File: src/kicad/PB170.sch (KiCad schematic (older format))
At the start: 51 parts, among them J2 USB_B_Micro, Q1 BC817, Q2 BC817, Q3 BC817, Q4 BC817, SW1 SW_MEC_5E, U1 74HC08, U20 74LS73, U21 74LS73

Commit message: Partially fixed footprint library and reassigning references
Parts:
- C1: footprint Capacitors_SMD:C_0805 -> Capacitor_SMD:C_0805_2012Metric
- C2: footprint Capacitors_SMD:C_1206 -> Capacitor_SMD:C_1206_3216Metric
- C3: footprint Capacitors_SMD:C_0805 -> Capacitor_SMD:C_0805
- D1: footprint Housings_SSOP:TSSOP-14_4.4x5mm_Pitch0.65mm -> Housing_SSOP:TSSOP-14_4.4x5mm_Pitch0.65mm
- D2, DB1, DB2, DB3, DG1, DG2, DG3, DR1, DR2, DR3: footprint LEDs:LED_0603 -> LED_SMD:LED_0603_1608Metric
- DY1, DY2, DY3: footprint LEDs:LED_0603 -> LED:LED_0603
- O1, O2, O3, U1: footprint Housings_SOIC:SOIC-14_3.9x8.7mm_Pitch1.27mm -> Housing_SOIC:SOIC-14_3.9x8.7mm_Pitch1.27mm
- Q1, Q2, Q3, Q4: footprint TO_SOT_Packages_SMD:SOT-23 -> TO_SOT_Package_SMD:SOT-23
- R1, R3, R5, R8, RB1, RB2, RG1, RG3, RY1, RY2, RY3: footprint Resistors_SMD:R_0603 -> Resistor_SMD:R_0603
- R11, R2, R4, R6, R7: footprint Resistors_SMD:R_0603 -> Resistor_SMD:R_0603_1608Metric
- RG2: footprint Resistors_SMD:R_0603 -> (none)
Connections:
- net 555output: now also U20.5 (C), U21.5 (C)
- net GND: now also C2.2
- net JK1Q: no longer C3.1, C3.2, D2.2 (A), J2.1 (VBUS), N555.4 (R), N555.8 (VCC), Q1.3 (C), Q2.3 (C), Q3.3 (C), Q4.3 (C), R4.1, SW1.1, SW1.2, SW1.3 (K), SW1.4 (A), U20.10 (K), U20.5 (C), U20.7 (J), U21.10 (K), U21.5 (C)
- net at R6.2: now also C3.1, D2.2 (A), J2.1 (VBUS), N555.4 (R), N555.8 (VCC), Q1.3 (C), Q2.3 (C), Q3.3 (C), Q4.3 (C), R4.1, SW1.3 (K), SW1.4 (A), U20.10 (K), U21.10 (K)
- new net: C3.2, SW1.1, SW1.2, U20.7 (J)

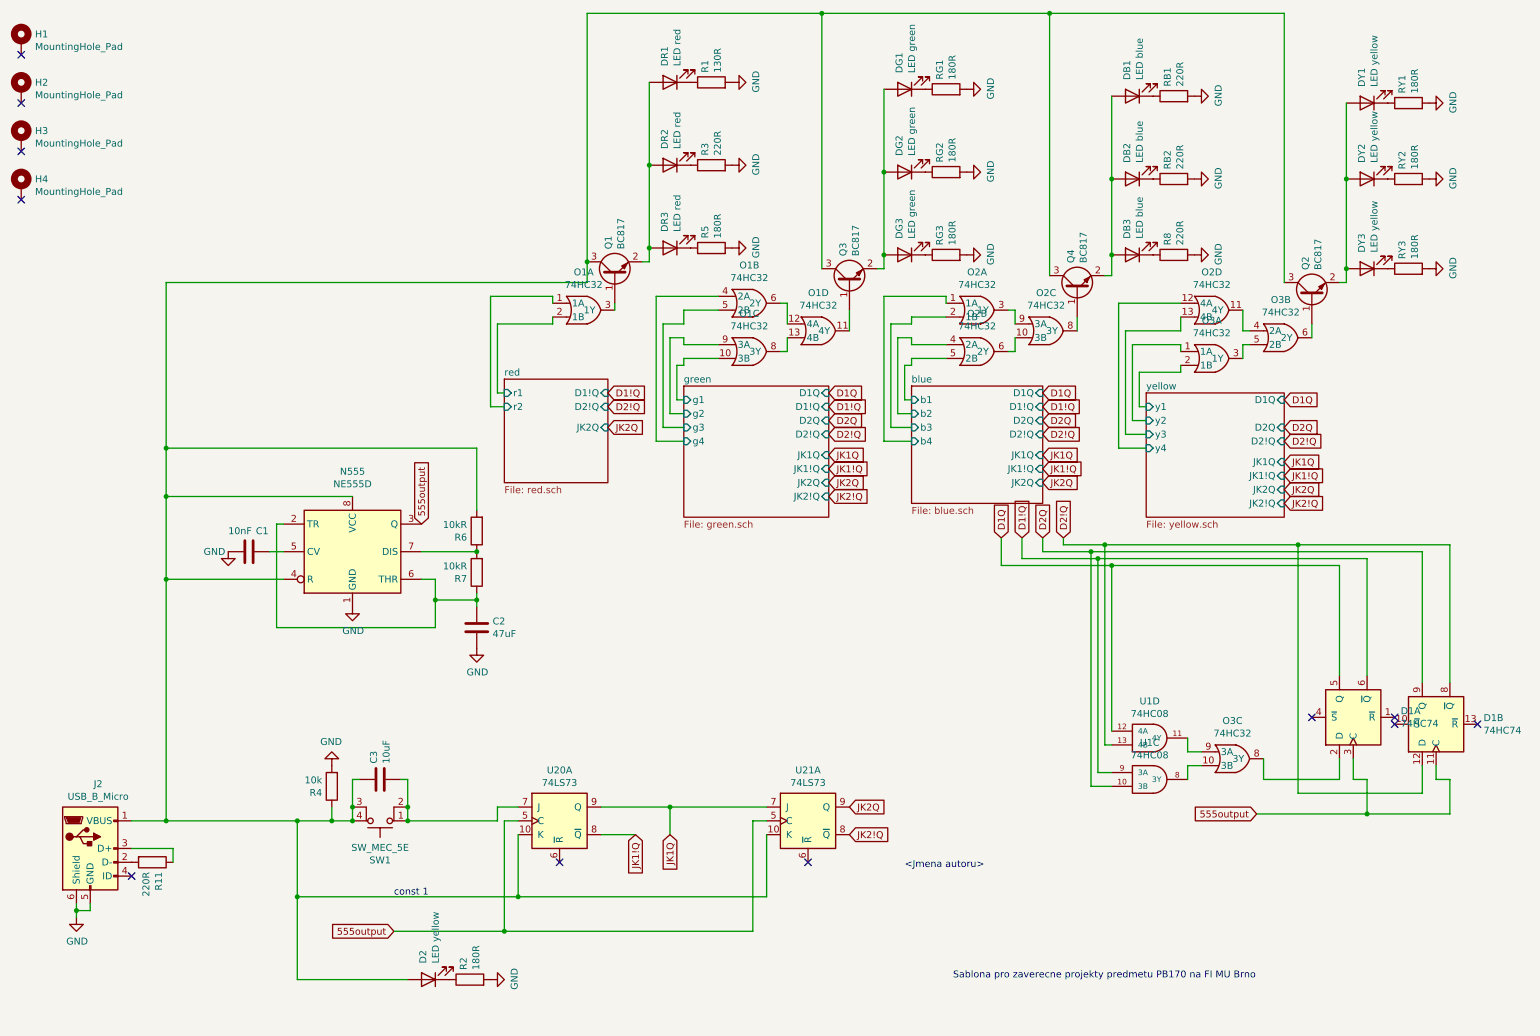
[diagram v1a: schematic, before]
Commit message: added annotations, power connections to parts
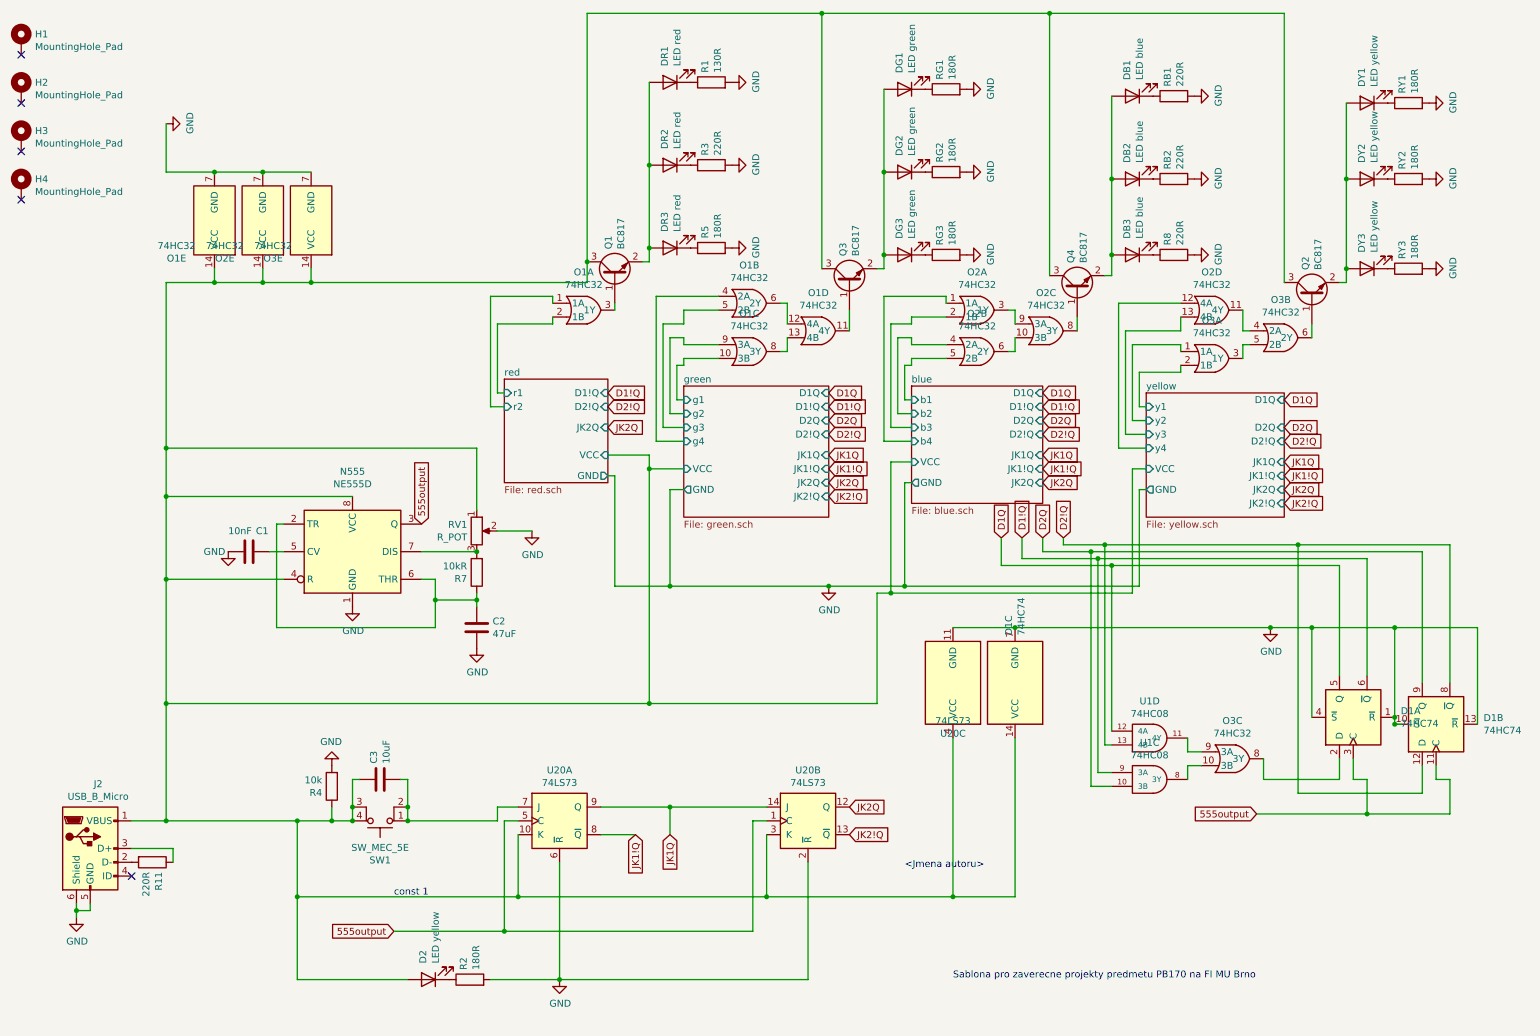
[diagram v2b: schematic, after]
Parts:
- removed R6: 10kR, Resistor_SMD:R_0603_1608Metric, symbol Device:R
- added unit 3 of D1
- added unit 5 of O1
- added unit 5 of O2
- added unit 5 of O3
- added RV1: R_POT, PB170:potentiometer10k, symbol Device:R_POT
- added unit 3 of U20
- C3: footprint Capacitor_SMD:C_0805 -> Capacitor_SMD:C_0805_2012Metric
- D1: footprint Housing_SSOP:TSSOP-14_4.4x5mm_Pitch0.65mm -> Package_SO:HTSSOP-14-1EP_4.4x5mm_P0.65mm_EP3.4x5mm_Mask3x3.1mm
- DY1, DY2, DY3: footprint LED:LED_0603 -> LED_SMD:LED_0603_1608Metric
- J2: footprint PB170:USB_Micro-B_Wuerth_629105150521_CircularHoles -> PB170:MICRO-USB-SMD_MICROXNJ; LCSC (none) -> C404969
- O1, O2, O3, U1: footprint Housing_SOIC:SOIC-14_3.9x8.7mm_Pitch1.27mm -> Package_SO:SOIC-14_3.9x8.7mm_P1.27mm
- Q1, Q2, Q3, Q4: footprint TO_SOT_Package_SMD:SOT-23 -> Package_TO_SOT_SMD:SOT-23
- R1, R3, R5, R8, RB1, RB2, RG1, RG3, RY1, RY2, RY3: footprint Resistor_SMD:R_0603 -> Resistor_SMD:R_0603_1608Metric
- RG2: footprint (none) -> Resistor_SMD:R_0603_1608Metric
- renumbered U21 to U20
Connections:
- net 555output: now also U20.1 (C); no longer U20.5 (C)
- net GND: now also D1.1 (~R), D1.10 (~S), D1.13 (~R), D1.4 (~S), U20.2 (~R), U20.6 (~R), D1.7 (GND), O1.7 (GND), O2.7 (GND), O3.7 (GND), RV1.2, U20.11 (GND)
- net JK1Q: now also U20.14 (J); no longer U20.7 (J)
- net JK2!Q: now also U20.13 (~Q); no longer U20.8 (~Q)
- net JK2Q: now also U20.12 (Q); no longer U20.9 (Q)
- net blue/VCC: now reaches C3.1, D2.2 (A), J2.1 (VBUS), N555.4 (R), N555.8 (VCC), Q1.3 (C), Q2.3 (C), Q3.3 (C), Q4.3 (C), R4.1, SW1.3 (K), SW1.4 (A), U20.10 (K)
- net blue/VCC: now also U20.3 (K), D1.14 (VCC), O1.14 (VCC), O2.14 (VCC), O3.14 (VCC), RV1.1, U20.4 (VCC); no longer U20.10 (K)
- net at N555.7 (DIS), R7.2: now also RV1.3
- no-connect marks 11 -> 5

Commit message: finished eeschema
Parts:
- removed U20: 74LS73, symbol 74xx:74LS73
- added U21: 74HC08, Package_SO:SOIC-14_3.9x8.7mm_P1.27mm, symbol PB170:74HC08
- added U22: 74HC74, Package_SO:HTSSOP-14-1EP_4.4x5mm_P0.65mm_EP3.4x5mm_Mask3x3.1mm, symbol 74xx:74HC74
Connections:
- net 555output: now also U22.11 (C), U22.3 (C)
- net GND: now also U21.7 (GND), U22.12 (D), U22.2 (D), U22.7 (GND)
- net JK1!Q: now also U21.2 (1B), U22.6 (~Q)
- net JK1Q: now also U21.4 (2A), U21.9 (3A), U22.5 (Q)
- net JK2!Q: now also U21.10 (3B), U22.8 (~Q)
- net JK2Q: now also U21.12 (4A), U22.9 (Q)
- net blue/VCC: now also U21.13 (4B), U21.14 (VCC), U21.5 (2B), U22.14 (VCC)
- net at C3.2, SW1.1, SW1.2: now also U21.1 (1A)
- new net: U21.6 (2Y), U22.1 (~R)
- new net: U21.3 (1Y), U22.4 (~S)
- new net: U21.8 (3Y), U22.10 (~S)
- new net: U21.11 (4Y), U22.13 (~R)
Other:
- moved on the sheet: D2, R2
